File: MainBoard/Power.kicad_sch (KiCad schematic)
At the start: 48 parts, among them J1 1769, U11 XC6206P302MR_C5148691, U4 BQ27220YZFR, U6 EA3036C, U7 MT3608, U9 BQ24074RGTR

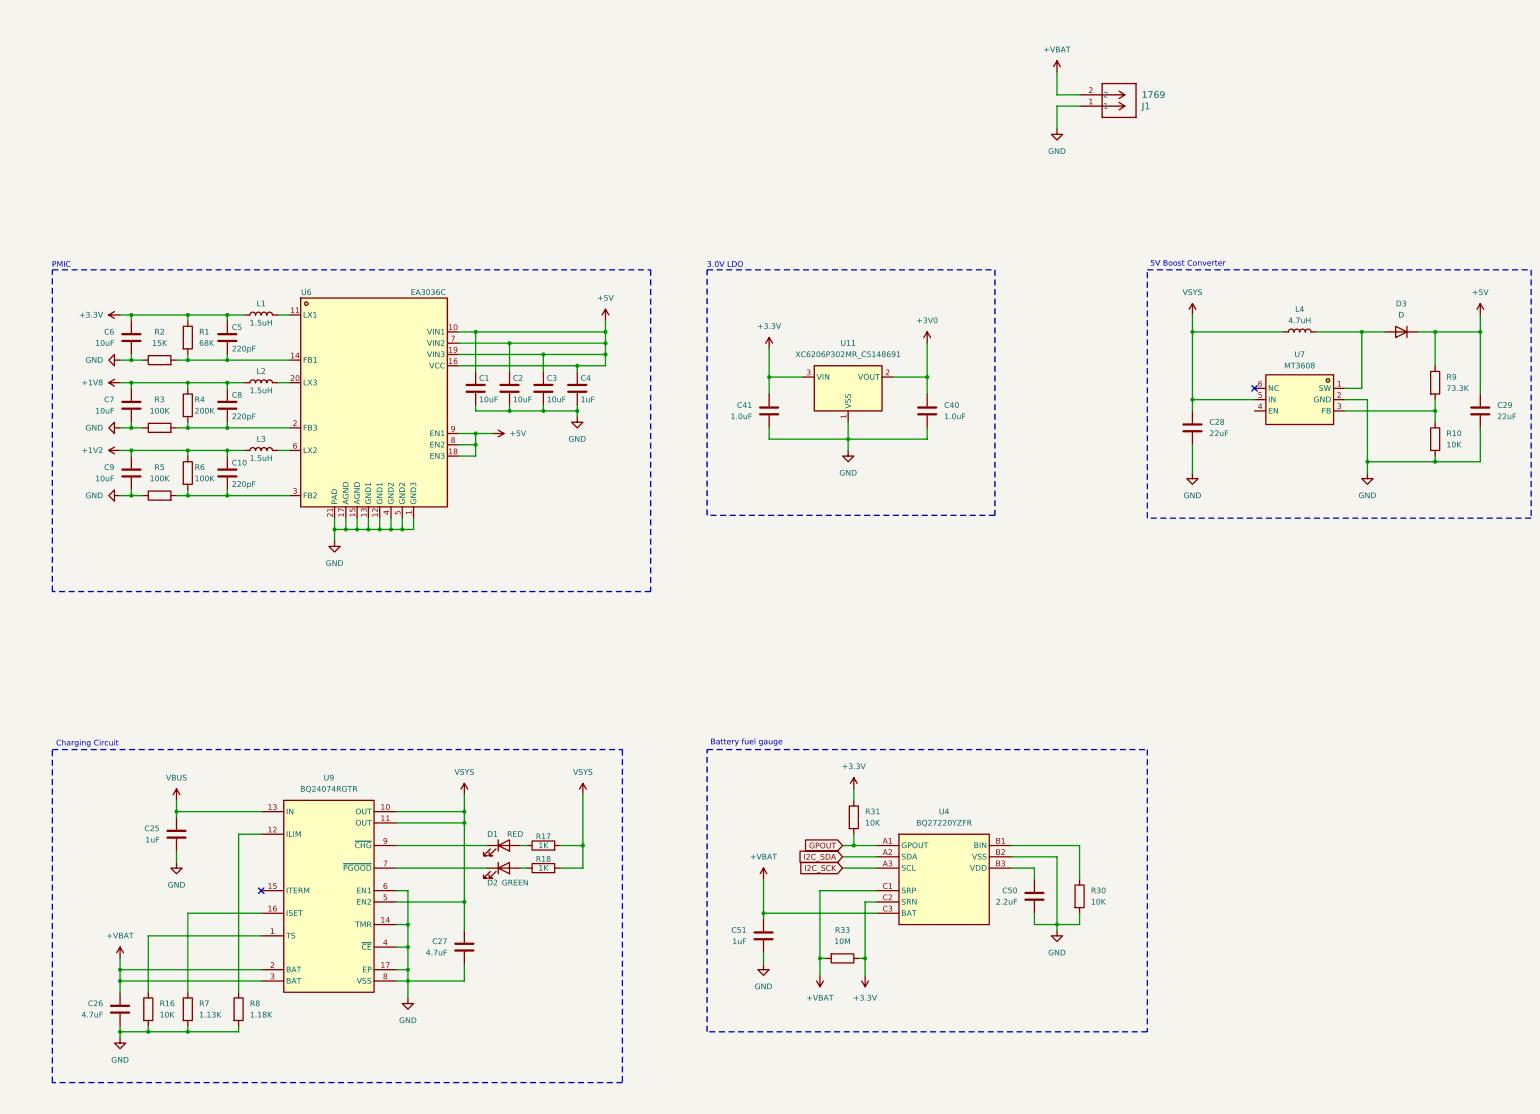
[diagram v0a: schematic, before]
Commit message: footprints for wheel + power changes for v3s
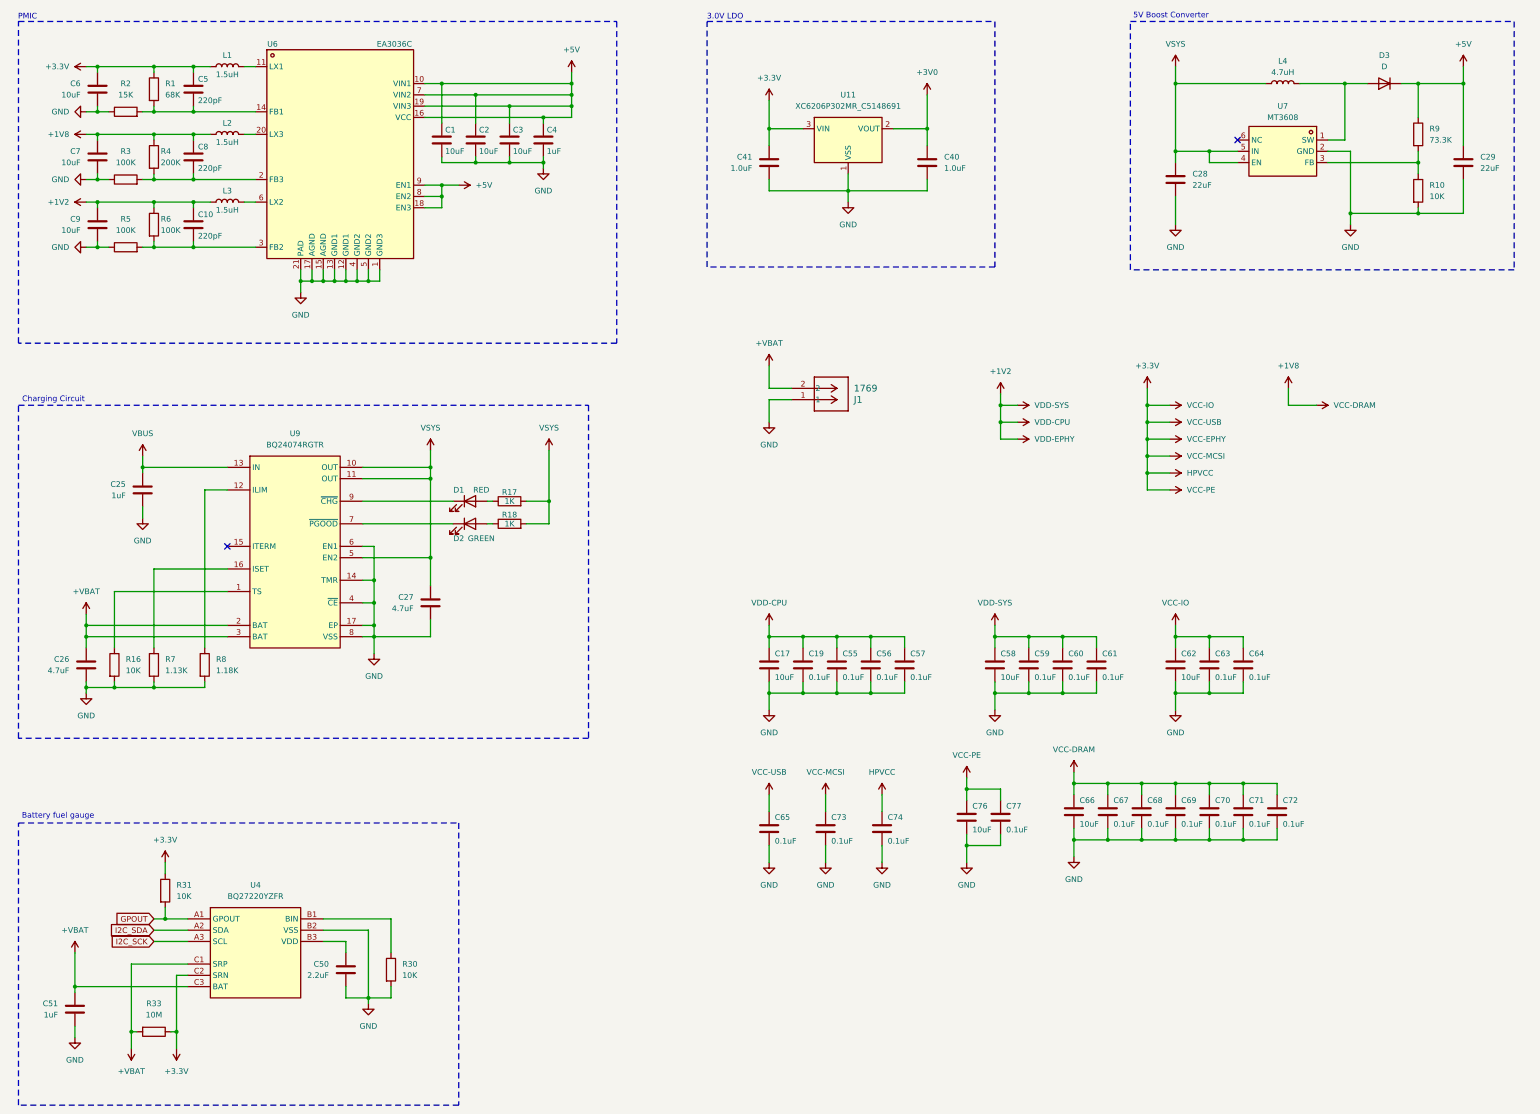
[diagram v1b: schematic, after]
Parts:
- added C17, C58, C62, C66, C76: 10uF, symbol Device:C
- added C19, C55, C56, C57, C59, C60, C61, C63, C64, C65, C67, C68, C69, C70, C71, C72, C73, C74, C77: 0.1uF, symbol Device:C
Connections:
- net +1V2: now also C17.1, C19.1, C55.1, C56.1, C57.1, C58.1, C59.1, C60.1, C61.1
- net +1V8: now also C66.1, C67.1, C68.1, C69.1, C70.1, C71.1, C72.1
- net +3.3V: now also C62.1, C63.1, C64.1, C65.1, C73.1, C74.1, C76.1, C77.1
- net GND: now also C17.2, C19.2, C55.2, C56.2, C57.2, C58.2, C59.2, C60.2, C61.2, C62.2, C63.2, C64.2, C65.2, C66.2, C67.2, C68.2, C69.2, C70.2, C71.2, C72.2, C73.2, C74.2, C76.2, C77.2
- net VSYS: now also U7.4 (EN)
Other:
- moved on the sheet: C1, C10, C2, C25, C26, C27, C28, C29, C3, C4, C40, C41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

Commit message: minor power changes
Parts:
- C1, C17, C2, C28, C29, C3, C58, C6, C62, C66, C7, C76: footprint (none) -> Capacitor_SMD:C_0603_1608Metric
- C10, C19, C25, C26, C27, C4, C40, C41, C5, C50, C51, C55, C56, C57, C59, C60, C61, C63, C64, C65, C67, C68, C69, C70, C71, C72, C73, C74, C77, C8, C9: footprint (none) -> Capacitor_SMD:C_0402_1005Metric
- D1, D2: footprint (none) -> LED_SMD:LED_0402_1005Metric
- D3: footprint (none) -> Diode_SMD:D_0603_1608Metric
- L1, L2, L3, L4: footprint (none) -> Inductor_SMD:L_0402_1005Metric
- R1, R10, R16, R17, R18, R2, R3, R30, R31, R33, R4, R5, R6, R7, R8, R9: footprint (none) -> Resistor_SMD:R_0402_1005Metric
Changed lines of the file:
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@@
 			)
 		)
-		(property "Footprint" ""
+		(property "Footprint" "Capacitor_SMD:C_0603_1608Metric"
 			(at 238.4552 207.01 0)
 			(effects
@@
 			)
 		)
-		(property "Footprint" ""
+		(property "Footprint" "Capacitor_SMD:C_0402_1005Metric"
 			(at 270.2052 205.74 0)
 			(effects
@@
 			)
 		)
-		(property "Footprint" ""
+		(property "Footprint" "Resistor_SMD:R_0402_1005Metric"
 			(at 52.832 54.61 90)
 			(effects
@@
 			)
 		)
-		(property "Footprint" ""
+		(property "Footprint" "Capacitor_SMD:C_0603_1608Metric"
 			(at 194.0052 172.72 0)
 			(effects
@@
 			)
 		)
-		(property "Footprint" ""
+		(property "Footprint" "Capacitor_SMD:C_0402_1005Metric"
 			(at 143.2052 54.61 0)
 			(effects
@@
 			)
 		)
-		(property "Footprint" ""
+		(property "Footprint" "Capacitor_SMD:C_0402_1005Metric"
 			(at 293.0652 205.74 0)
 			(effects
@@
 			)
 		)
-		(property "Footprint" ""
+		(property "Footprint" "Capacitor_SMD:C_0402_1005Metric"
 			(at 267.6652 172.72 0)
 			(effects
@@
 			)
 		)
-		(property "Footprint" ""
+		(property "Footprint" "Capacitor_SMD:C_0402_1005Metric"
 			(at 37.7952 250.19 0)
 			(effects
@@
 			)
 		)
-		(property "Footprint" ""
+		(property "Footprint" "Resistor_SMD:R_0402_1005Metric"
 			(at 48.26 61.468 90)
 			(effects
@@
 			)
 		)
-		(property "Footprint" ""
+		(property "Footprint" "LED_SMD:LED_0402_1005Metric"
 			(at 125.73 137.16 0)
 			(effects
@@
 			)
 		)
-		(property "Footprint" ""
+		(property "Footprint" "Capacitor_SMD:C_0402_1005Metric"
 			(at 117.8052 158.75 0)
 			(effects
@@
 			)
 		)
-		(property "Footprint" ""
+		(property "Footprint" "Resistor_SMD:R_0402_1005Metric"
 			(at 134.62 133.858 90)
 			(effects
@@
 			)
 		)
-		(property "Footprint" ""
+		(property "Footprint" "Capacitor_SMD:C_0603_1608Metric"
 			(at 40.9448 58.42 0)
 			(effects
@@
 			)
 		)
-		(property "Footprint" ""
+		(property "Footprint" "Capacitor_SMD:C_0402_1005Metric"
 			(at 277.8252 205.74 0)
 			(effects
@@
 			)
 		)
-		(property "Footprint" ""
+		(property "Footprint" "Resistor_SMD:R_0402_1005Metric"
 			(at 134.62 138.938 90)
 			(effects
@@
 			)
 		)
-		(property "Footprint" ""
+		(property "Footprint" "Capacitor_SMD:C_0402_1005Metric"
 			(at 98.7552 241.3 0)
 			(effects
@@
 			)
 		)
-		(property "Footprint" ""
+		(property "Footprint" "Capacitor_SMD:C_0402_1005Metric"
 			(at 300.6852 205.74 0)
 			(effects
@@
 			)
 		)
-		(property "Footprint" ""
+		(property "Footprint" "Capacitor_SMD:C_0603_1608Metric"
 			(at 285.4452 172.72 0)
 			(effects
@@
 			)
 		)
-		(property "Footprint" ""
+		(property "Footprint" "Resistor_SMD:R_0402_1005Metric"
 			(at 64.262 168.91 90)
 			(effects
@@
 			)
 		)
-		(property "Footprint" ""
+		(property "Footprint" "Capacitor_SMD:C_0402_1005Metric"
 			(at 40.3352 172.72 0)
 			(effects
@@
 			)
 		)
-		(property "Footprint" ""
+		(property "Footprint" "Capacitor_SMD:C_0402_1005Metric"
 			(at 206.7052 209.55 0)
 			(effects
@@
 			)
 		)
-		(property "Footprint" ""
+		(property "Footprint" "Capacitor_SMD:C_0402_1005Metric"
 			(at 53.0352 133.35 0)
 			(effects
@@
 			)
 		)
-		(property "Footprint" ""
+		(property "Footprint" "Inductor_SMD:L_0402_1005Metric"
 			(at 71.12 64.77 0)
 			(effects
@@
 			)
 		)
-		(property "Footprint" ""
+		(property "Footprint" "Capacitor_SMD:C_0402_1005Metric"
 			(at 209.2452 172.72 0)
 			(effects
@@
 			)
 		)
-		(property "Footprint" ""
+		(property "Footprint" "Capacitor_SMD:C_0402_1005Metric"
 			(at 246.0752 207.01 0)
 			(effects
@@
 			)
 		)
-		(property "Footprint" ""
+		(property "Footprint" "Resistor_SMD:R_0402_1005Metric"
 			(at 54.61 249.682 90)
 			(effects
@@
 			)
 		)
-		(property "Footprint" ""
+		(property "Footprint" "Capacitor_SMD:C_0603_1608Metric"
 			(at 120.3452 54.61 0)
 			(effects
@@
 			)
 		)
-		(property "Footprint" ""
+		(property "Footprint" "Capacitor_SMD:C_0402_1005Metric"
 			(at 40.9448 73.66 0)
 			(effects
@@
 			)
 		)
-		(property "Footprint" ""
+		(property "Footprint" "Resistor_SMD:R_0402_1005Metric"
 			(at 106.172 237.49 90)
 			(effects
@@
 			)
 		)
-		(property "Footprint" ""
+		(property "Footprint" "Capacitor_SMD:C_0402_1005Metric"
 			(at 308.3052 205.74 0)
 			(effects
@@
 			)
 		)
-		(property "Footprint" ""
+		(property "Footprint" "Resistor_SMD:R_0402_1005Metric"
 			(at 55.372 219.71 90)
 			(effects
@@
 			)
 		)
-		(property "Footprint" ""
+		(property "Footprint" "Capacitor_SMD:C_0402_1005Metric"
 			(at 64.4652 58.42 0)
 			(effects
@@
 			)
 		)
-		(property "Footprint" ""
+		(property "Footprint" "Capacitor_SMD:C_0402_1005Metric"
 			(at 201.6252 172.72 0)
 			(effects
@@
 			)
 		)
-		(property "Footprint" ""
+		(property "Footprint" "Resistor_SMD:R_0402_1005Metric"
 			(at 48.26 46.228 90)
 			(effects
@@
 			)
 		)
-		(property "Footprint" ""
+		(property "Footprint" "Diode_SMD:D_0603_1608Metric"
 			(at 331.47 38.1 0)
 			(effects
@@
 			)
 		)
-		(property "Footprint" ""
+		(property "Footprint" "Resistor_SMD:R_0402_1005Metric"
 			(at 337.312 62.23 90)
 			(effects
@@
 			)
 		)
-		(property "Footprint" ""
+		(property "Footprint" "Inductor_SMD:L_0402_1005Metric"
 			(at 71.12 34.29 0)
 			(effects
@@
 			)
 		)
-		(property "Footprint" ""
+		(property "Footprint" "Capacitor_SMD:C_0603_1608Metric"
 			(at 350.2152 59.69 0)
 			(effects
@@
 			)
 		)
-		(property "Footprint" ""
+		(property "Footprint" "Capacitor_SMD:C_0402_1005Metric"
 			(at 219.4052 209.55 0)
 			(effects
@@
 			)
 		)
-		(property "Footprint" ""
+		(property "Footprint" "Resistor_SMD:R_0402_1005Metric"
 			(at 337.312 49.53 90)
 			(effects
@@
 			)
 		)
-		(property "Footprint" ""
+		(property "Footprint" "Capacitor_SMD:C_0402_1005Metric"
 			(at 252.4252 172.72 0)
 			(effects
@@
 			)
 		)
-		(property "Footprint" ""
+		(property "Footprint" "Capacitor_SMD:C_0603_1608Metric"
 			(at 244.8052 172.72 0)
 			(effects
@@
 			)
 		)
-		(property "Footprint" ""
+		(property "Footprint" "Capacitor_SMD:C_0402_1005Metric"
 			(at 192.0748 59.69 0)
 			(effects
@@
 			)
 		)
-		(property "Footprint" ""
+		(property "Footprint" "Capacitor_SMD:C_0603_1608Metric"
 			(at 40.9448 43.18 0)
 			(effects
@@
 			)
 		)
-		(property "Footprint" ""
+		(property "Footprint" "Capacitor_SMD:C_0603_1608Metric"
 			(at 285.4452 63.5 0)
 			(effects
@@
 			)
 		)
-		(property "Footprint" ""
+		(property "Footprint" "Capacitor_SMD:C_0402_1005Metric"
 			(at 260.0452 172.72 0)
 			(effects
@@
 			)
 		)
-		(property "Footprint" ""
+		(property "Footprint" "Resistor_SMD:R_0402_1005Metric"
 			(at 52.832 168.91 90)
 			(effects
@@
 			)
 		)
-		(property "Footprint" ""
+		(property "Footprint" "Capacitor_SMD:C_0402_1005Metric"
 			(at 300.6852 172.72 0)
 			(effects
@@
 			)
 		)
-		(property "Footprint" ""
+		(property "Footprint" "Capacitor_SMD:C_0402_1005Metric"
 			(at 229.5652 59.69 0)
 			(effects
@@
 			)
 		)
-		(property "Footprint" ""
+		(property "Footprint" "Capacitor_SMD:C_0402_1005Metric"
 			(at 285.4452 205.74 0)
 			(effects
@@
 			)
 		)
-		(property "Footprint" ""
+		(property "Footprint" "Capacitor_SMD:C_0603_1608Metric"
 			(at 135.5852 54.61 0)
 			(effects
@@
 			)
 		)
-		(property "Footprint" ""
+		(property "Footprint" "Capacitor_SMD:C_0402_1005Metric"
 			(at 64.4652 43.18 0)
 			(effects
@@
 			)
 		)
-		(property "Footprint" ""
+		(property "Footprint" "Resistor_SMD:R_0402_1005Metric"
 			(at 48.26 76.708 90)
 			(effects
@@
 			)
 		)
-		(property "Footprint" ""
+		(property "Footprint" "Capacitor_SMD:C_0402_1005Metric"
 			(at 64.4652 73.66 0)
 			(effects
@@
 			)
 		)
-		(property "Footprint" ""
+		(property "Footprint" "Capacitor_SMD:C_0603_1608Metric"
 			(at 262.5852 205.74 0)
 			(effects
@@
 			)
 		)
-		(property "Footprint" ""
+		(property "Footprint" "Capacitor_SMD:C_0402_1005Metric"
 			(at 216.8652 172.72 0)
 			(effects
@@
 			)
 		)
-		(property "Footprint" ""
+		(property "Footprint" "Capacitor_SMD:C_0603_1608Metric"
 			(at 127.9652 54.61 0)
 			(effects
@@
 			)
 		)
-		(property "Footprint" ""
+		(property "Footprint" "Resistor_SMD:R_0402_1005Metric"
 			(at 43.942 168.91 90)
 			(effects
@@
 			)
 		)
-		(property "Footprint" ""
+		(property "Footprint" "Inductor_SMD:L_0402_1005Metric"
 			(at 308.61 38.1 0)
 			(effects
@@
 			)
 		)
-		(property "Footprint" ""
+		(property "Footprint" "LED_SMD:LED_0402_1005Metric"
 			(at 125.73 132.08 0)
 			(effects
@@
 			)
 		)
-		(property "Footprint" ""
+		(property "Footprint" "Resistor_SMD:R_0402_1005Metric"
 			(at 52.832 69.85 90)
 			(effects
@@
 			)
 		)
-		(property "Footprint" ""
+		(property "Footprint" "Resistor_SMD:R_0402_1005Metric"
 			(at 52.832 39.37 90)
 			(effects
@@
 			)
 		)
-		(property "Footprint" ""
+		(property "Footprint" "Capacitor_SMD:C_0402_1005Metric"
 			(at 293.0652 172.72 0)
 			(effects
@@
 			)
 		)
-		(property "Footprint" ""
+		(property "Footprint" "Capacitor_SMD:C_0402_1005Metric"
 			(at 194.0052 209.55 0)
 			(effects
@@
 			)
 		)
-		(property "Footprint" ""
+		(property "Footprint" "Inductor_SMD:L_0402_1005Metric"
 			(at 71.12 49.53 0)
 			(effects
@@
 			)
 		)
-		(property "Footprint" ""
+		(property "Footprint" "Capacitor_SMD:C_0402_1005Metric"
 			(at 224.4852 172.72 0)
 			(effects

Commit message: layout and starting routing
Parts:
- C9: footprint Capacitor_SMD:C_0402_1005Metric -> Capacitor_SMD:C_0603_1608Metric
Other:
- note added: "FIGURE OUT THIS DIODE"
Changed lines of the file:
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@@
 		)
 	)
+	(text "FIGURE OUT THIS DIODE"
+		(exclude_from_sim no)
+		(at 332.232 41.148 0)
+		(effects
+			(font
+				(size 1.27 1.27)
+			)
+		)
+	)
 	(text "5V Boost Converter"
 		(exclude_from_sim no)
@@
 			)
 		)
-		(property "Footprint" "Capacitor_SMD:C_0402_1005Metric"
+		(property "Footprint" "Capacitor_SMD:C_0603_1608Metric"
 			(at 40.9448 73.66 0)
 			(effects

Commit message: starting to route
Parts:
- removed C74: 0.1uF, Capacitor_SMD:C_0402_1005Metric, symbol Device:C
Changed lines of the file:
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@@
 	(wire
 		(pts
-			(xy 218.44 198.12) (xy 218.44 201.93)
-		)
-		(stroke
-			(width 0)
-			(type default)
-		)
-	)
-	(wire
-		(pts
 			(xy 223.52 175.26) (xy 215.9 175.26)
 		)
@@
 	(wire
 		(pts
-			(xy 218.44 209.55) (xy 218.44 213.36)
-		)
-		(stroke
-			(width 0)
-			(type default)
-		)
-	)
-	(wire
-		(pts
 			(xy 349.25 67.31) (xy 339.09 67.31)
 		)
@@
 	)
 	(symbol
-		(lib_id "Device:C")
-		(at 218.44 205.74 0)
-		(unit 1)
-		(exclude_from_sim no)
-		(in_bom yes)
-		(on_board yes)
-		(dnp no)
-		(property "Reference" "C74"
-			(at 219.71 203.2 0)
-			(effects
-				(font
-					(size 1.27 1.27)
-				)
-				(justify left)
-			)
-		)
-		(property "Value" "0.1uF"
-			(at 219.71 208.534 0)
-			(effects
-				(font
-					(size 1.27 1.27)
-				)
-				(justify left)
-			)
-		)
-		(property "Footprint" "Capacitor_SMD:C_0402_1005Metric"
-			(at 219.4052 209.55 0)
-			(effects
-				(font
-					(size 1.27 1.27)
-				)
-				(hide yes)
-			)
-		)
-		(property "Datasheet" "~"
-			(at 218.44 205.74 0)
-			(effects
-				(font
-					(size 1.27 1.27)
-				)
-				(hide yes)
-			)
-		)
-		(property "Description" "Unpolarized capacitor"
-			(at 218.44 205.74 0)
-			(effects
-				(font
-					(size 1.27 1.27)
-				)
-				(hide yes)
-			)
-		)
-		(pin "1"
-		)
-		(pin "2"
-		)
-		(instances
-			(project "MainBoard"
-				(path "/8a2ca4d7-9471-417b-a346-3246fc9a2f27/f6d58287-0bbb-4a4e-8690-1e10380d899b"
-					(reference "C74")
-					(unit 1)
-				)
-			)
-		)
-	)
-	(symbol
 		(lib_id "power:+1V2")
 		(at 283.21 110.49 270)
@@
 	)
 	(symbol
-		(lib_id "power:+1V2")
-		(at 218.44 198.12 0)
-		(unit 1)
-		(exclude_from_sim no)
-		(in_bom yes)
-		(on_board yes)
-		(dnp no)
-		(fields_autoplaced yes)
-		(property "Reference" "#PWR0152"
-			(at 218.44 201.93 0)
-			(effects
-				(font
-					(size 1.27 1.27)
-				)
-				(hide yes)
-			)
-		)
-		(property "Value" "HPVCC"
-			(at 218.44 193.04 0)
-			(effects
-				(font
-					(size 1.27 1.27)
-				)
-			)
-		)
-		(property "Footprint" ""
-			(at 218.44 198.12 0)
-			(effects
-				(font
-					(size 1.27 1.27)
-				)
-				(hide yes)
-			)
-		)
-		(property "Datasheet" ""
-			(at 218.44 198.12 0)
-			(effects
-				(font
-					(size 1.27 1.27)
-				)
-				(hide yes)
-			)
-		)
-		(property "Description" "Power symbol creates a global label with name \"+1V2\""
-			(at 218.44 198.12 0)
-			(effects
-				(font
-					(size 1.27 1.27)
-				)
-				(hide yes)
-			)
-		)
-		(pin "1"
-		)
-		(instances
-			(project "MainBoard"
-				(path "/8a2ca4d7-9471-417b-a346-3246fc9a2f27/f6d58287-0bbb-4a4e-8690-1e10380d899b"
-					(reference "#PWR0152")
-					(unit 1)
-				)
-			)
-		)
-	)
-	(symbol
 		(lib_id "Device:R")
 		(at 339.09 49.53 0)
@@
 					(unit 1)
 				)
-			)
-		)
-	)
-	(symbol
-		(lib_id "power:GND")
-		(at 218.44 213.36 0)
-		(unit 1)
-		(exclude_from_sim no)
-		(in_bom yes)
-		(on_board yes)
-		(dnp no)
-		(fields_autoplaced yes)
-		(property "Reference" "#PWR017"
-			(at 218.44 219.71 0)
-			(effects
-				(font
-					(size 1.27 1.27)
-				)
-				(hide yes)
-			)
-		)
-		(property "Value" "GND"
-			(at 218.44 218.44 0)
-			(effects
-				(font
-					(size 1.27 1.27)
-				)
-			)
-		)
-		(property "Footprint" ""
-			(at 218.44 213.36 0)
-			(effects
-				(font
-					(size 1.27 1.27)
-				)
-				(hide yes)
-			)
-		)
-		(property "Datasheet" ""
-			(at 218.44 213.36 0)
-			(effects
-				(font
-					(size 1.27 1.27)
-				)
-				(hide yes)
-			)
-		)
-		(property "Description" "Power symbol creates a global label with name \"GND\" , ground"
-			(at 218.44 213.36 0)
-			(effects
-				(font
-					(size 1.27 1.27)
-				)
-				(hide yes)
-			)
-		)
-		(pin "1"
-		)
-		(instances
-			(project "MainBoard"
-				(path "/8a2ca4d7-9471-417b-a346-3246fc9a2f27/f6d58287-0bbb-4a4e-8690-1e10380d899b"
-					(reference "#PWR017")
-					(unit 1)
-				)
